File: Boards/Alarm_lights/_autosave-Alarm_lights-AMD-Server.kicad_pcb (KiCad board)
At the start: 2 copper layers, 63 x 107.6 mm, 60 parts, among them J1 PinsLeft, J2 PinsRight, J3 JST, J4 PinsBottom, Q1 BC547, Q10 BC547, Q11 BC547, Q12 BC547, Q13 BC547, Q14 BC547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

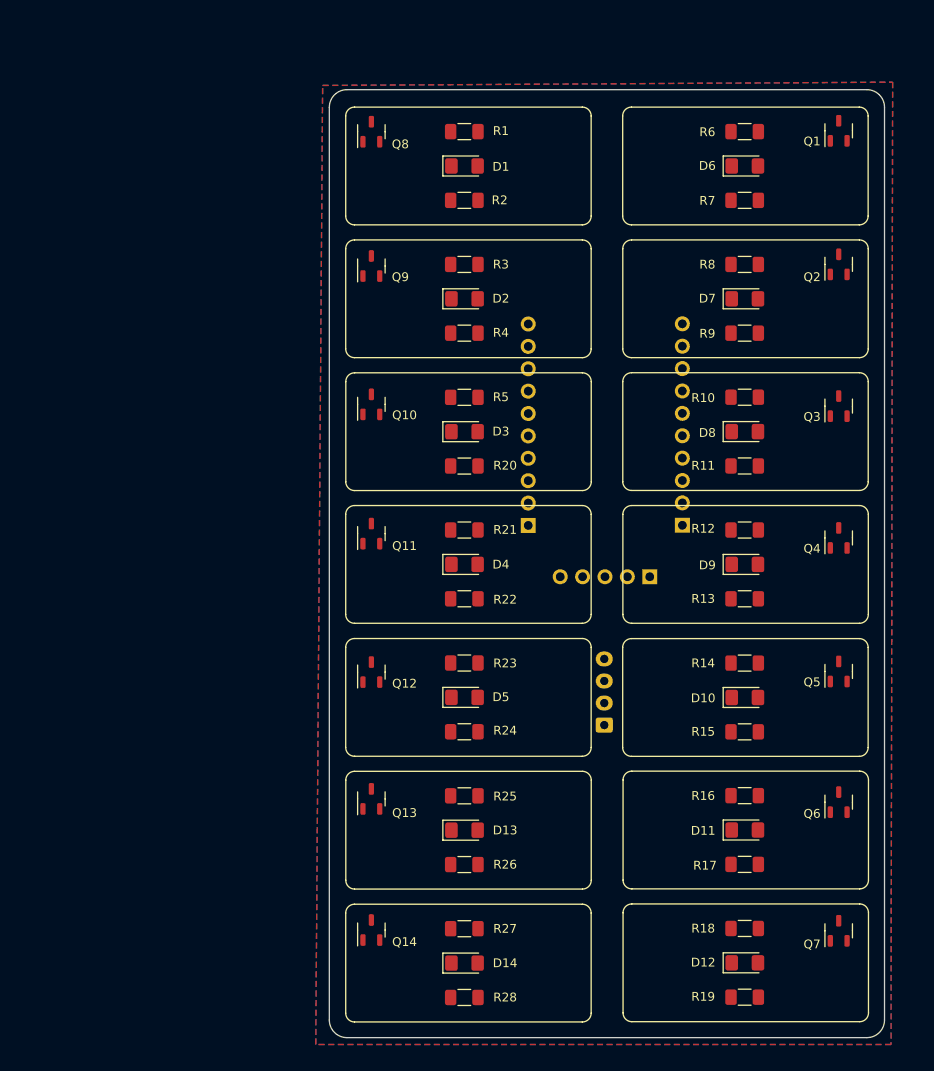
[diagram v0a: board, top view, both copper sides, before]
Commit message: Update Alarm lights pcb to use BJT's, a different IO Expander, and fit correctly into f3d assembly
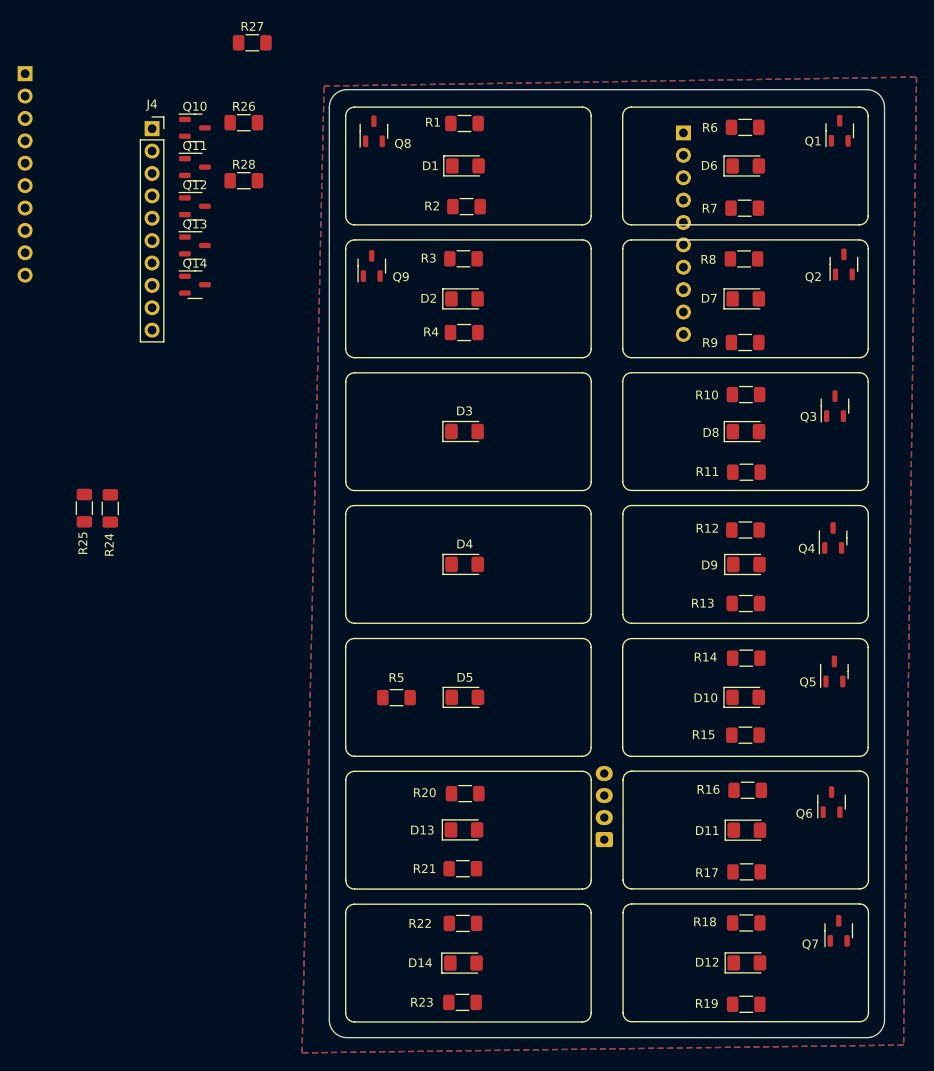
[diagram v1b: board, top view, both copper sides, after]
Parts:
- J4: footprint Connector_PinSocket_2.54mm:PinSocket_1x05_P2.54mm_Vertical -> Connector_PinSocket_2.54mm:PinSocket_1x10_P2.54mm_Vertical; moved to F.Cu
- moved R27 103.4 mm to (119.6, 27.3), turned to 0 degrees
- moved R28 96.0 mm to (118.7, 43.0), turned to 0 degrees
- moved R26 87.8 mm to (118.7, 36.4), turned to 0 degrees
- moved J2 76.7 mm to (93.8, 30.9), turned to 180 degrees
- moved J4 76.0 mm to (108.3, 37.1), turned to 0 degrees
- moved Q14 75.9 mm to (113.1, 54.8), turned to 0 degrees
- moved Q13 65.9 mm to (113.1, 50.3), turned to 0 degrees
- moved Q12 56.5 mm to (113.1, 45.9), turned to 0 degrees
- moved R25 54.1 mm to (100.6, 80.2), turned to 90 degrees
- moved R24 47.5 mm to (103.5, 80.2), turned to 90 degrees
- moved Q11 46.2 mm to (113.1, 41.4), turned to 0 degrees
- moved J1 44.5 mm to (168.6, 37.6), turned to 180 degrees
- moved R23 38.5 mm to (143.5, 136.2), turned to 0 degrees
- moved R21 38.4 mm to (143.5, 121.1), turned to 0 degrees
- moved Q10 37.2 mm to (113.1, 37.0), turned to 0 degrees
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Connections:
- J1 pad 1: GND -> Uplink
- J1 pad 10: Uplink -> GND
- J1 pad 2: unconnected-(J1-Pin_2-Pad2) -> No Att
- J1 pad 3: unconnected-(J1-Pin_3-Pad3) -> STBY
- J1 pad 4: Prio Disp -> Key Rel
- J1 pad 5: No Dap -> Opr Err
- J1 pad 6: Opr Err -> No Dap
- J1 pad 7: Key Rel -> Prio Disp
- J1 pad 8: STBY -> unconnected-(J1-Pin_8-Pad8)
- J1 pad 9: No Att -> unconnected-(J1-Pin_9-Pad9)
- J2 pad 1: GND -> Temp
- J2 pad 10: Temp -> unconnected-(J2-Pin_10-Pad10)
- J2 pad 2: unconnected-(J2-Pin_2-Pad2) -> Gimbal Lock
- J2 pad 3: unconnected-(J2-Pin_3-Pad3) -> Prog
- J2 pad 4: Vel -> Restart
- J2 pad 5: Alt -> Tracker
- J2 pad 6: Tracker -> Alt
- J2 pad 7: Restart -> Vel
- J2 pad 8: Prog -> unconnected-(J2-Pin_8-Pad8)
- J2 pad 9: Gimbal Lock -> unconnected-(J2-Pin_9-Pad9)
- J4 pad 1: GND -> unconnected-(J4-Pin_1-Pad1)
- J4 pad 2: +5V -> SCK
- J4 pad 4: SCK -> +5V
- J4 pad 5: unconnected-(J4-Pin_5-Pad5) -> GND
